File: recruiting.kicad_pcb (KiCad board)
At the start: 2 copper layers, 62.5 x 62 mm, 54 parts, among them Q1 IRF9383M, Q2 IRF9383M, U1 LM25085MM, U2 LM25085MM, U3 LM358

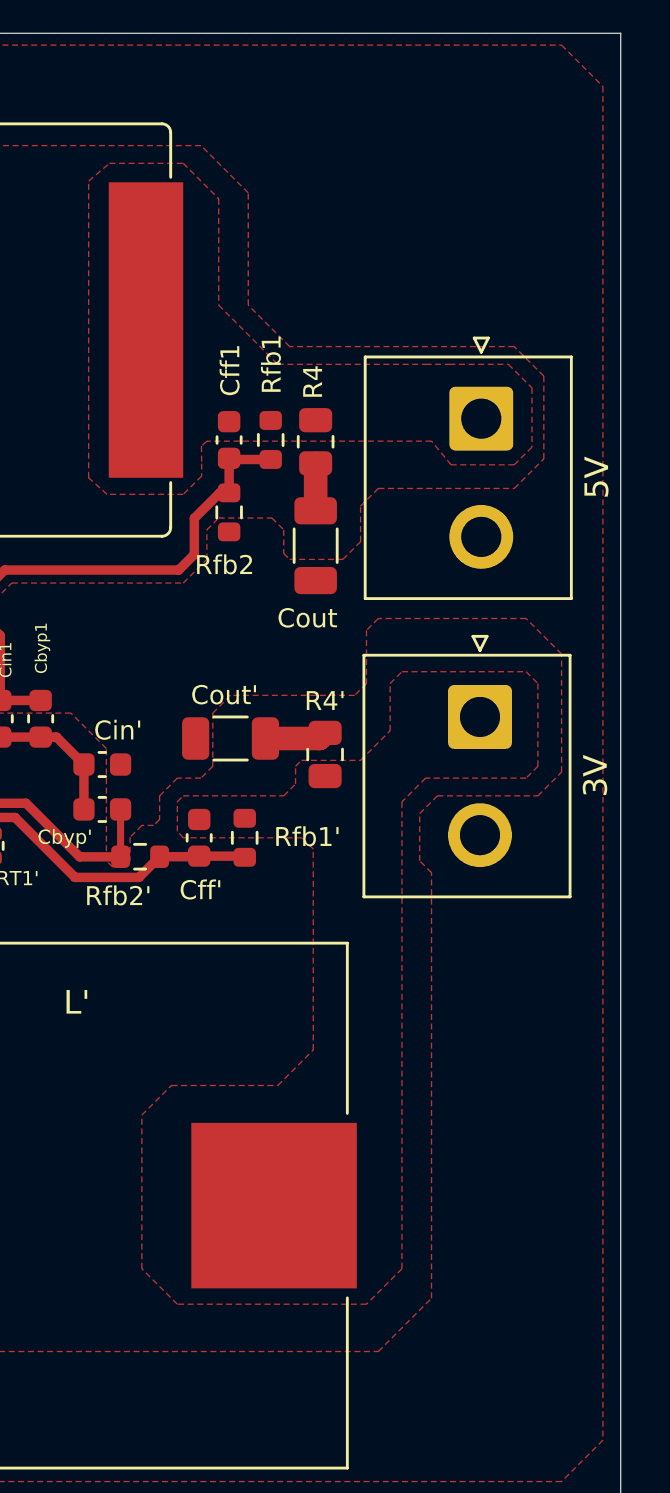
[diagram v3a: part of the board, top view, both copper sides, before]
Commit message: condensatori riposizionati
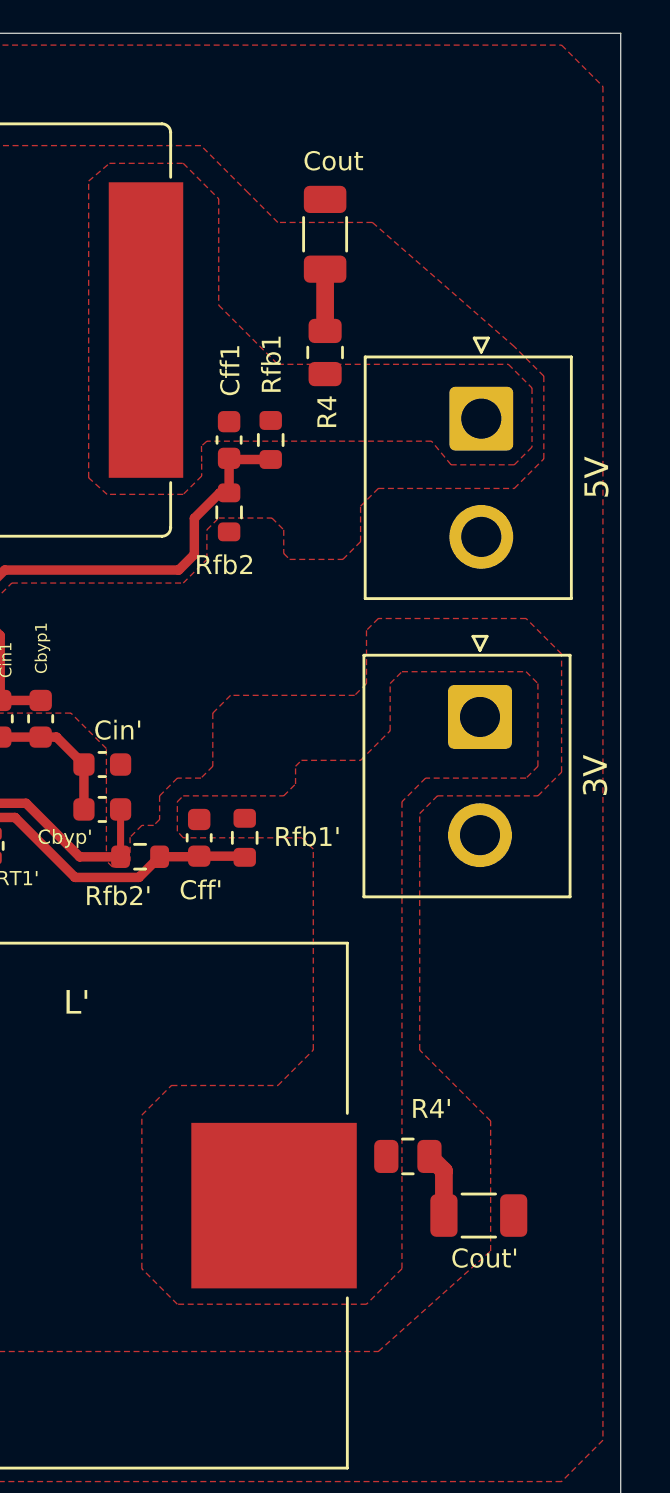
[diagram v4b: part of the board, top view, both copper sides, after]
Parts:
- moved Cout' 22.7 mm to (161.0, 117.0), turned to 0 degrees
- moved R4' 17.4 mm to (158.0, 114.5), turned to 0 degrees
- moved Cout 13.2 mm to (154.5, 75.5), turned to 90 degrees
- moved R4 3.80 mm to (154.5, 80.5), turned to 90 degrees
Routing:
- net Net-(Cout1-Pad1): track 2.01 -> 2.61 mm
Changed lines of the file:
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@@
   )
   (footprint "Capacitor_SMD:C_1206_3216Metric" (layer "F.Cu")
-    (at 150.5 96.825 180)
+    (at 161 117)
     (descr "Capacitor SMD 1206 (3216 Metric), square (rectangular) end terminal, IPC_7351 nominal, (Body size source: IPC-SM-782 page 76, https://www.pcb-3d.com/wordpress/wp-content/uploads/ipc-sm-782a_amendment_1_and_2.pdf), generated with kicad-footprint-generator")
     (tags "capacitor")
@@
     (fp_line (start -1.6 -0.8) (end 1.6 -0.8) (layer "F.Fab") (width 0.1))
     (fp_line (start 1.6 -0.8) (end 1.6 0.8) (layer "F.Fab") (width 0.1))
-    (pad "1" smd roundrect (at -1.475 0 180) (size 1.15 1.8) (layers "F.Cu" "F.Paste" "F.Mask") (roundrect_rratio 0.2173913043)
+    (pad "1" smd roundrect (at -1.475 0) (size 1.15 1.8) (layers "F.Cu" "F.Paste" "F.Mask") (roundrect_rratio 0.2173913043)
       (net 10 "Net-(Cout'1-Pad1)") (pintype "passive"))
-    (pad "2" smd roundrect (at 1.475 0 180) (size 1.15 1.8) (layers "F.Cu" "F.Paste" "F.Mask") (roundrect_rratio 0.2173913043)
+    (pad "2" smd roundrect (at 1.475 0) (size 1.15 1.8) (layers "F.Cu" "F.Paste" "F.Mask") (roundrect_rratio 0.2173913043)
       (net 1 "GND") (pintype "passive"))
     (model "${KICAD6_3DMODEL_DIR}/Capacitor_SMD.3dshapes/C_1206_3216Metric.wrl"
@@
   )
   (footprint "Resistor_SMD:R_0805_2012Metric" (layer "F.Cu")
-    (at 154.5 97.5 90)
+    (at 158 114.5)
     (descr "Resistor SMD 0805 (2012 Metric), square (rectangular) end terminal, IPC_7351 nominal, (Body size source: IPC-SM-782 page 72, https://www.pcb-3d.com/wordpress/wp-content/uploads/ipc-sm-782a_amendment_1_and_2.pdf), generated with kicad-footprint-generator")
     (tags "resistor")
@@
     (property "Sheetname" "")
     (attr smd)
-    (fp_text reference "R4'" (at 2.25 0 180) (layer "F.SilkS")
+    (fp_text reference "R4'" (at 1 -2 180) (layer "F.SilkS")
       (effects (font (size 0.8 0.8) (thickness 0.15)))
     )
-    (fp_text value "1,2 Ω" (at 0 1.65 90) (layer "F.Fab")
-      (effects (font (size 1 1) (thickness 0.15)))
-    )
-    (fp_text user "${REFERENCE}" (at 0 0 90) (layer "F.Fab")
+    (fp_text value "1,2 Ω" (at 0 1.65) (layer "F.Fab")
+      (effects (font (size 1 1) (thickness 0.15)))
+    )
+    (fp_text user "${REFERENCE}" (at 0 0) (layer "F.Fab")
       (effects (font (size 0.5 0.5) (thickness 0.08)))
     )
@@
     (fp_line (start -1 0.625) (end -1 -0.625) (layer "F.Fab") (width 0.1))
     (fp_line (start 1 0.625) (end -1 0.625) (layer "F.Fab") (width 0.1))
-    (pad "1" smd roundrect (at -0.9125 0 90) (size 1.025 1.4) (layers "F.Cu" "F.Paste" "F.Mask") (roundrect_rratio 0.243902439)
+    (pad "1" smd roundrect (at -0.9125 0) (size 1.025 1.4) (layers "F.Cu" "F.Paste" "F.Mask") (roundrect_rratio 0.243902439)
       (net 6 "3,3V0,5A") (pintype "passive"))
-    (pad "2" smd roundrect (at 0.9125 0 90) (size 1.025 1.4) (layers "F.Cu" "F.Paste" "F.Mask") (roundrect_rratio 0.243902439)
+    (pad "2" smd roundrect (at 0.9125 0) (size 1.025 1.4) (layers "F.Cu" "F.Paste" "F.Mask") (roundrect_rratio 0.243902439)
       (net 10 "Net-(Cout'1-Pad1)") (pintype "passive"))
     (model "${KICAD6_3DMODEL_DIR}/Resistor_SMD.3dshapes/R_0805_2012Metric.wrl"
@@
   )
   (footprint "Resistor_SMD:R_0805_2012Metric" (layer "F.Cu")
-    (at 154.09952 84.275 -90)
+    (at 154.5 80.5 90)
     (descr "Resistor SMD 0805 (2012 Metric), square (rectangular) end terminal, IPC_7351 nominal, (Body size source: IPC-SM-782 page 72, https://www.pcb-3d.com/wordpress/wp-content/uploads/ipc-sm-782a_amendment_1_and_2.pdf), generated with kicad-footprint-generator")
     (tags "resistor")
@@
     (property "Sheetname" "")
     (attr smd)
-    (fp_text reference "R4" (at -2.525 0.09952 -90) (layer "F.SilkS")
+    (fp_text reference "R4" (at -2.525 0.09952 90) (layer "F.SilkS")
       (effects (font (size 0.8 0.8) (thickness 0.15)))
     )
@@
     (fp_line (start -1 -0.625) (end 1 -0.625) (layer "F.Fab") (width 0.1))
     (fp_line (start 1 -0.625) (end 1 0.625) (layer "F.Fab") (width 0.1))
-    (pad "1" smd roundrect (at -0.9125 0 270) (size 1.025 1.4) (layers "F.Cu" "F.Paste" "F.Mask") (roundrect_rratio 0.243902439)
+    (pad "1" smd roundrect (at -0.9125 0 90) (size 1.025 1.4) (layers "F.Cu" "F.Paste" "F.Mask") (roundrect_rratio 0.243902439)
       (net 8 "5V3A") (pintype "passive"))
-    (pad "2" smd roundrect (at 0.9125 0 270) (size 1.025 1.4) (layers "F.Cu" "F.Paste" "F.Mask") (roundrect_rratio 0.243902439)
+    (pad "2" smd roundrect (at 0.9125 0 90) (size 1.025 1.4) (layers "F.Cu" "F.Paste" "F.Mask") (roundrect_rratio 0.243902439)
       (net 11 "Net-(Cout1-Pad1)") (pintype "passive"))
     (model "${KICAD6_3DMODEL_DIR}/Resistor_SMD.3dshapes/R_0805_2012Metric.wrl"
@@
   )
   (footprint "Capacitor_SMD:C_1206_3216Metric" (layer "F.Cu")
-    (at 154.1 88.67 -90)
+    (at 154.5 75.5 90)
     (descr "Capacitor SMD 1206 (3216 Metric), square (rectangular) end terminal, IPC_7351 nominal, (Body size source: IPC-SM-782 page 76, https://www.pcb-3d.com/wordpress/wp-content/uploads/ipc-sm-782a_amendment_1_and_2.pdf), generated with kicad-footprint-generator")
     (tags "capacitor")
@@
     (property "Sheetname" "")
     (attr smd)
-    (fp_text reference "Cout" (at 3.08 0.35 180) (layer "F.SilkS")
+    (fp_text reference "Cout" (at 3.08 0.35) (layer "F.SilkS")
       (effects (font (size 0.8 0.8) (thickness 0.15)))
     )
@@
     (fp_line (start 1.6 -0.8) (end 1.6 0.8) (layer "F.Fab") (width 0.1))
     (fp_line (start 1.6 0.8) (end -1.6 0.8) (layer "F.Fab") (width 0.1))
-    (pad "1" smd roundrect (at -1.475 0 270) (size 1.15 1.8) (layers "F.Cu" "F.Paste" "F.Mask") (roundrect_rratio 0.2173913043)
+    (pad "1" smd roundrect (at -1.475 0 90) (size 1.15 1.8) (layers "F.Cu" "F.Paste" "F.Mask") (roundrect_rratio 0.2173913043)
       (net 11 "Net-(Cout1-Pad1)") (pintype "passive"))
-    (pad "2" smd roundrect (at 1.475 0 270) (size 1.15 1.8) (layers "F.Cu" "F.Paste" "F.Mask") (roundrect_rratio 0.2173913043)
+    (pad "2" smd roundrect (at 1.475 0 90) (size 1.15 1.8) (layers "F.Cu" "F.Paste" "F.Mask") (roundrect_rratio 0.2173913043)
       (net 1 "GND") (pintype "passive"))
     (model "${KICAD6_3DMODEL_DIR}/Capacitor_SMD.3dshapes/C_1206_3216Metric.wrl"
@@
   (segment (start 150.43952 84.97548) (end 150.43952 86.43548) (width 0.4) (layer "F.Cu") (net 9))
   (segment (start 138 90.5) (end 140.15096 90.5) (width 0.4) (layer "F.Cu") (net 9))
-  (segment (start 151.975 96.825) (end 154.2625 96.825) (width 1) (layer "F.Cu") (net 10))
-  (segment (start 154.2625 96.825) (end 154.5 96.5875) (width 1) (layer "F.Cu") (net 10))
-  (segment (start 154.09952 85.1875) (end 154.09952 87.19452) (width 1) (layer "F.Cu") (net 11))
-  (segment (start 154.09952 87.19452) (end 154.1 87.195) (width 1) (layer "F.Cu") (net 11))
+  (segment (start 159.525 117) (end 159.525 115.1125) (width 0.75) (layer "F.Cu") (net 10))
+  (segment (start 159.525 115.1125) (end 158.9125 114.5) (width 0.75) (layer "F.Cu") (net 10))
+  (segment (start 154.5 79.5875) (end 154.5 76.975) (width 0.75) (layer "F.Cu") (net 11))
   (segment (start 126.06 94.5825) (end 126.0525 94.575) (width 0.3) (layer "F.Cu") (net 12))
   (segment (start 121.8075 101.4825) (end 124.16 99.13) (width 1.5) (layer "F.Cu") (net 12))
@@
         (xy 133 122.75)
         (xy 156.75 122.75)
-        (xy 159 120.5)
-        (xy 159 102.5)
+        (xy 161.5 118.5)
+        (xy 161.5 113)
+        (xy 158.5 110)
         (xy 158.5 102)
         (xy 158.5 100)
@@
         (xy 163.75 81.5)
         (xy 162.5 80.25)
-        (xy 153 80.25)
-        (xy 151.25 78.5)
+        (xy 156.5 75)
+        (xy 152.5 75)
         (xy 151.25 73.75)
         (xy 149.25 71.75)

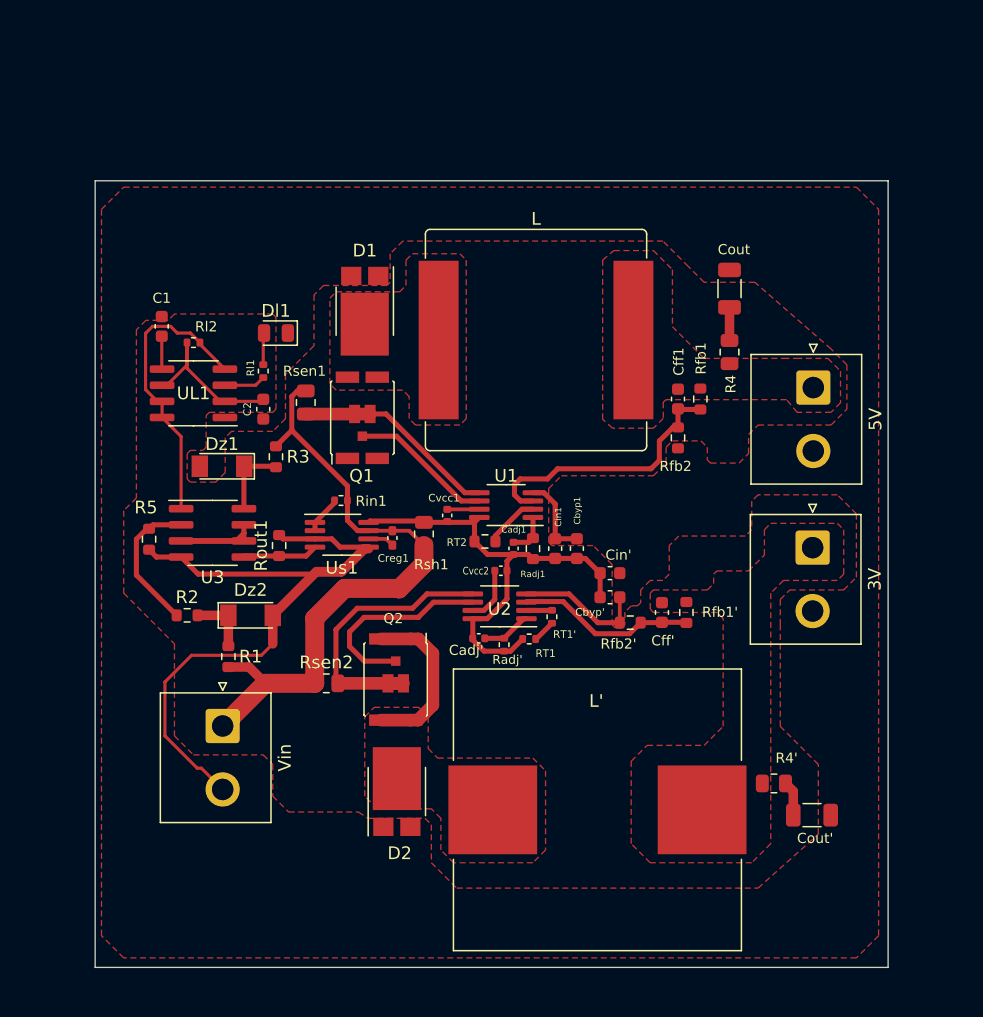
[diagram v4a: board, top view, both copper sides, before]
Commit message: modificalo lo schematic e rifatto in parte il design PCB
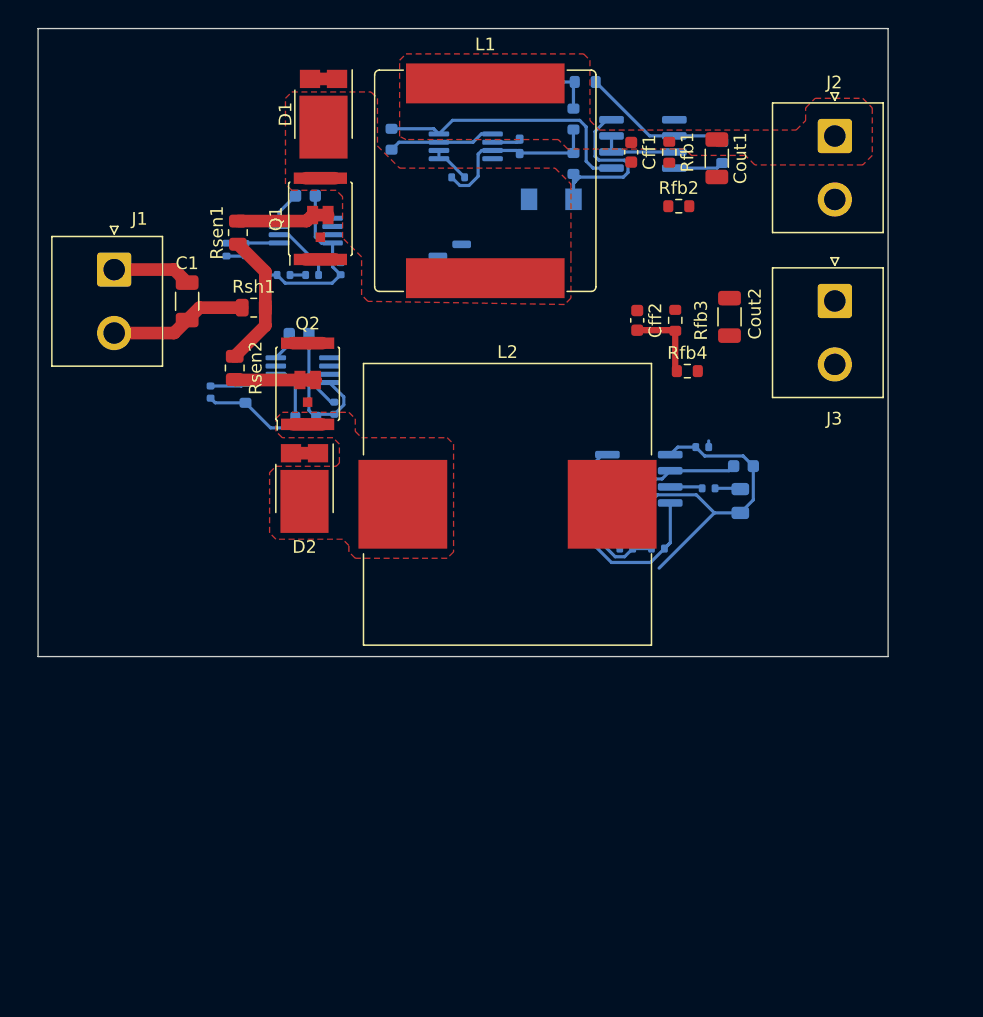
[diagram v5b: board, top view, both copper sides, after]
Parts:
- removed 3V, 5V, Vin: JST_NV_B02P-NV_1x02_P5.00mm_Vertical, Connector_JST:JST_NV_B02P-NV_1x02_P5.00mm_Vertical
- removed Cadj': 1 nF, Capacitor_SMD:C_0402_1005Metric
- removed Cbyp': 1,8 uF, Capacitor_SMD:C_0603_1608Metric
- removed Cbyp1: 3,3 uF, Capacitor_SMD:C_0603_1608Metric
- removed Cff': 0,39 uF, Capacitor_SMD:C_0603_1608Metric
- removed Cin': 3,3uF, Capacitor_SMD:C_0603_1608Metric
- removed Cin1: 39uF, Capacitor_SMD:C_0603_1608Metric
- removed Cout: 68 nF, Capacitor_SMD:C_1206_3216Metric
- removed Cout': 150 nF, Capacitor_SMD:C_1206_3216Metric
- removed L: 56 uH, Inductor_SMD:L_Pulse_PA4344
- removed L': 330 uH, Inductor_SMD:L_Wuerth_HCI-2212
- removed R4': 1,2 Ω, Resistor_SMD:R_0805_2012Metric
- removed RT1': 3,3KΩ, Resistor_SMD:R_0402_1005Metric
- removed Radj': 180Ω, Resistor_SMD:R_0402_1005Metric
- removed Rfb1': 12KΩ, Resistor_SMD:R_0603_1608Metric
- removed Rfb2': 18KΩ, Resistor_SMD:R_0603_1608Metric
- removed Rl1: 330Ω, Resistor_SMD:R_0402_1005Metric
- removed Rl2: 120KΩ, Resistor_SMD:R_0402_1005Metric
- removed UL1: NE555D, Package_SO:SOIC-8_3.9x4.9mm_P1.27mm
- removed Us1: LTC6102xMS8, Package_SO:MSOP-8_3x3mm_P0.65mm
- added C3: 1uF, Capacitor_SMD:C_0603_1608Metric, B.Cu at (146.1, 94.2)
- added Cadj'1: 1 nF, Capacitor_SMD:C_0402_1005Metric, B.Cu at (116.3, 72.4)
- added Cb1: 30 uF, Capacitor_SMD:C_0603_1608Metric, B.Cu at (120.6, 79.1)
- added Cb2: 30 uF, Capacitor_SMD:C_0603_1608Metric, B.Cu at (121.1, 68.2)
- added Cff2: 1.8 uF, Capacitor_SMD:C_0603_1608Metric, F.Cu at (147.2, 78.0)
- added Cout1: 18 uF, Capacitor_SMD:C_1206_3216Metric, F.Cu at (153.5, 65.2)
- added Cout2: 18 uF, Capacitor_SMD:C_1206_3216Metric, F.Cu at (154.5, 77.7)
- added J1: Conn_01x02_Female, Connector_JST:JST_NV_B02P-NV_1x02_P5.00mm_Vertical, F.Cu at (106.0, 74.0)
- added J2: Conn_01x02_Female, Connector_JST:JST_NV_B02P-NV_1x02_P5.00mm_Vertical, F.Cu at (162.8, 63.5)
- added J3: Conn_01x02_Female, Connector_JST:JST_NV_B02P-NV_1x02_P5.00mm_Vertical, F.Cu at (162.8, 76.5)
- added L1: 56 uH, Inductor_SMD:L_Pulse_PA4344, F.Cu at (135.2, 67.0)
- added L2: 240 uH, Inductor_SMD:L_Wuerth_HCI-2212, F.Cu at (137.0, 92.5)
- added Q3: DMN2040U, Package_TO_SOT_SMD:SOT-23, B.Cu at (132.5, 73.0)
- added R6: 560Ω, Resistor_SMD:R_0603_1608Metric, B.Cu at (143.1, 59.2)
- added R7: 100Ω, Resistor_SMD:R_0603_1608Metric, B.Cu at (153.9, 64.8)
- added R8: 560Ω, Resistor_SMD:R_0603_1608Metric, B.Cu at (142.2, 65.6)
- added RT3: 3,3KΩ, Resistor_SMD:R_0402_1005Metric, B.Cu at (121.6, 74.4)
- added Radj2: 180Ω, Resistor_SMD:R_0402_1005Metric, B.Cu at (114.8, 72.4)
- added Rfb3: 12KΩ, Resistor_SMD:R_0603_1608Metric, F.Cu at (150.2, 78.0)
- added Rfb4: 18KΩ, Resistor_SMD:R_0603_1608Metric, F.Cu at (151.2, 82.0)
- added U4: LTC6102xMS8, Package_SO:MSOP-8_3x3mm_P0.65mm, B.Cu at (133.7, 64.3)
- added U5: NE555D, Package_SO:SOIC-8_3.9x4.9mm_P1.27mm, B.Cu at (147.4, 90.5)
- C1: value 10nF -> 390uF; footprint Capacitor_SMD:C_0603_1608Metric -> Capacitor_SMD:C_1206_3216Metric
- C2, Cadj1, Creg1, Cvcc1, Cvcc2, Dl1, Dz1, Dz2, Radj1, Rin1, Rout1, U1, U2, U3: moved to B.Cu
- Cff1: value 1,8 uF -> 1.8 uF
- R1: value 560 -> 10KΩ; footprint Resistor_SMD:R_0603_1608Metric -> Resistor_SMD:R_0402_1005Metric; moved to B.Cu
- R2, R3: value 560Ω -> 120KΩ; footprint Resistor_SMD:R_0603_1608Metric -> Resistor_SMD:R_0402_1005Metric; moved to B.Cu
- R4: value 180 mΩ -> 330Ω; footprint Resistor_SMD:R_0805_2012Metric -> Resistor_SMD:R_0402_1005Metric; moved to B.Cu
- R5: value 100Ω -> 560; moved to B.Cu
- RT1: value 47KΩ -> 82KΩ; footprint Resistor_SMD:R_0402_1005Metric -> Resistor_SMD:R_0603_1608Metric; moved to B.Cu
- RT2: value 82KΩ -> 47KΩ; footprint Resistor_SMD:R_0603_1608Metric -> Resistor_SMD:R_0402_1005Metric; moved to B.Cu
- moved Dz2 47.3 mm to (138.5, 59.2), turned to 180 degrees
- moved R5 47.1 mm to (142.2, 62.1)
- moved U3 45.7 mm to (147.7, 64.1), turned to 180 degrees
- moved R1 40.8 mm to (152.4, 88.0), turned to 180 degrees
- moved Dl1 38.9 mm to (155.4, 92.2), turned to 90 degrees
- moved C2 38.1 mm to (155.6, 89.5), turned to 180 degrees
- moved R2 37.5 mm to (148.9, 96.0), turned to 180 degrees
- moved Dz1 33.4 mm to (140.5, 68.5)
- moved U2 33.3 mm to (121.1, 70.9), turned to 0 degrees
- moved Rout1 33.2 mm to (127.9, 63.7), turned to -90 degrees
- moved Creg1 32.5 mm to (138.0, 64.3), turned to 90 degrees
- moved R3 28.5 mm to (146.4, 96.0), turned to 180 degrees
- moved Rin1 27.1 mm to (133.1, 66.7), turned to 0 degrees
- moved Cvcc2 27.0 mm to (123.8, 73.9), turned to 90 degrees
- moved Cadj1 26.9 mm to (113.6, 83.7)
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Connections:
- net FB_1 renamed /FB1
- net GATE_1 renamed /GATE1
- net GATE_2 renamed /GATE2
- net ISEN_1 renamed /ISEN1
- net ISEN_2 renamed /ISEN2
- C1 pad 1: GND -> /Shunt monitor/Rin-
- C1 pad 2: Net-(C1-Pad2) -> GND
- Cff1 pad 1: 5V3A -> Net-(Cff1-Pad1)
- Creg1 pad 1: Vin -> /Shunt monitor/Rin-
- R1 pad 1: Net-(Dz2-Pad1) -> /Shunt monitor/Vout
- R1 pad 2: Vin -> GND
- R2 pad 1: Net-(R2-Pad1) -> Net-(Q3-Pad2)
- R2 pad 2: Net-(Dz2-Pad1) -> Net-(R2-Pad2)
- R3 pad 1: Vin -> Net-(R2-Pad2)
- R3 pad 2: Net-(Dz1-Pad1) -> Net-(C2-Pad2)
- R4 pad 1: 5V3A -> Net-(Dl1-Pad2)
- R5 pad 1: Net-(R2-Pad1) -> Net-(Dz2-Pad1)
- R5 pad 2: GND -> /Shunt monitor/Rin-
- RT1 pad 2: Net-(RT1'1-Pad1) -> Net-(RT1-Pad2)
- Rfb1 pad 1: 5V3A -> Net-(Cff1-Pad1)
- Rin1 pad 1: Vin -> /Shunt monitor/Rin-
- Rsen1 pad 1: Vin -> /Buck controller/Vin_B
- Rsen2 pad 1: Vin -> /Buck controller/Vin_B
- Rsh1 pad 1: Vin -> /Shunt monitor/Rin-
- U1 pad 2: Net-(RT2-Pad2) -> Net-(RT1-Pad2)
- U2 pad 3: FB_2 -> /FB2
- U3 pad 2: Net-(R2-Pad1) -> Net-(R6-Pad1)
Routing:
- net Vin: track 50.6 -> 0.00 mm
- net /Shunt monitor/Rin-: track 0.00 -> 24.9 mm
- net /Shunt monitor/Vout: track 23.1 -> 0.87 mm
- net /FB1: track 21.4 -> 0.00 mm
- net Net-(Q3-Pad2): track 0.00 -> 20.5 mm
- net GND: track 75.6 -> 56.0 mm
- net /GATE2: track 15.9 -> 0.00 mm
- net Net-(Rout1-Pad1): track 5.93 -> 21.1 mm
- net /ISEN2: track 22.3 -> 7.60 mm
- net FB_2: track 14.1 -> 0.00 mm
- net /Buck controller/Vin_B: track 36.8 -> 49.8 mm
- net Net-(R6-Pad1): track 0.00 -> 11.9 mm
- net Net-(R2-Pad2): track 0.00 -> 11.8 mm
- net /GATE1: track 11.3 -> 0.00 mm
- net Net-(R2-Pad1): track 11.3 -> 0.00 mm
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- added copper zone on F.Cu, net (none)
- removed copper zone on F.Cu, net 3,3V0,5A
- removed copper zone on F.Cu, net 5V3A
- removed copper zone on F.Cu, net GND
- removed copper zone on F.Cu, net Net-(D1-Pad3)
- removed copper zone on F.Cu, net Net-(D2-Pad3)
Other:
- board size 62.5 x 62 mm -> 67 x 49.5 mm
